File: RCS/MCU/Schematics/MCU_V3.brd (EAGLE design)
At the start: 100 x 78.7 mm, 26 parts, among them IC1 FT232RL, Q2 8 MHz, U1 ATMEGA328P_TQFP, X1 USB-A

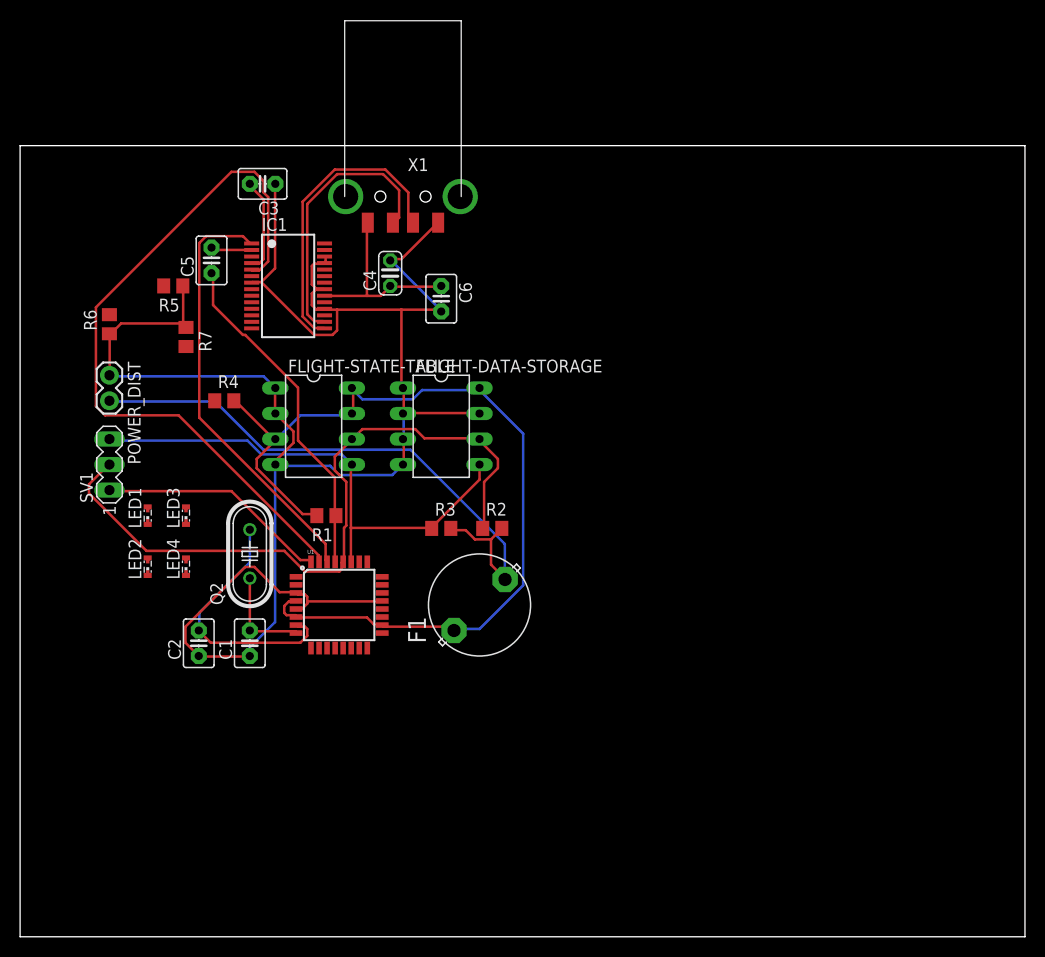
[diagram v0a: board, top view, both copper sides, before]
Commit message: Completed PCB layout
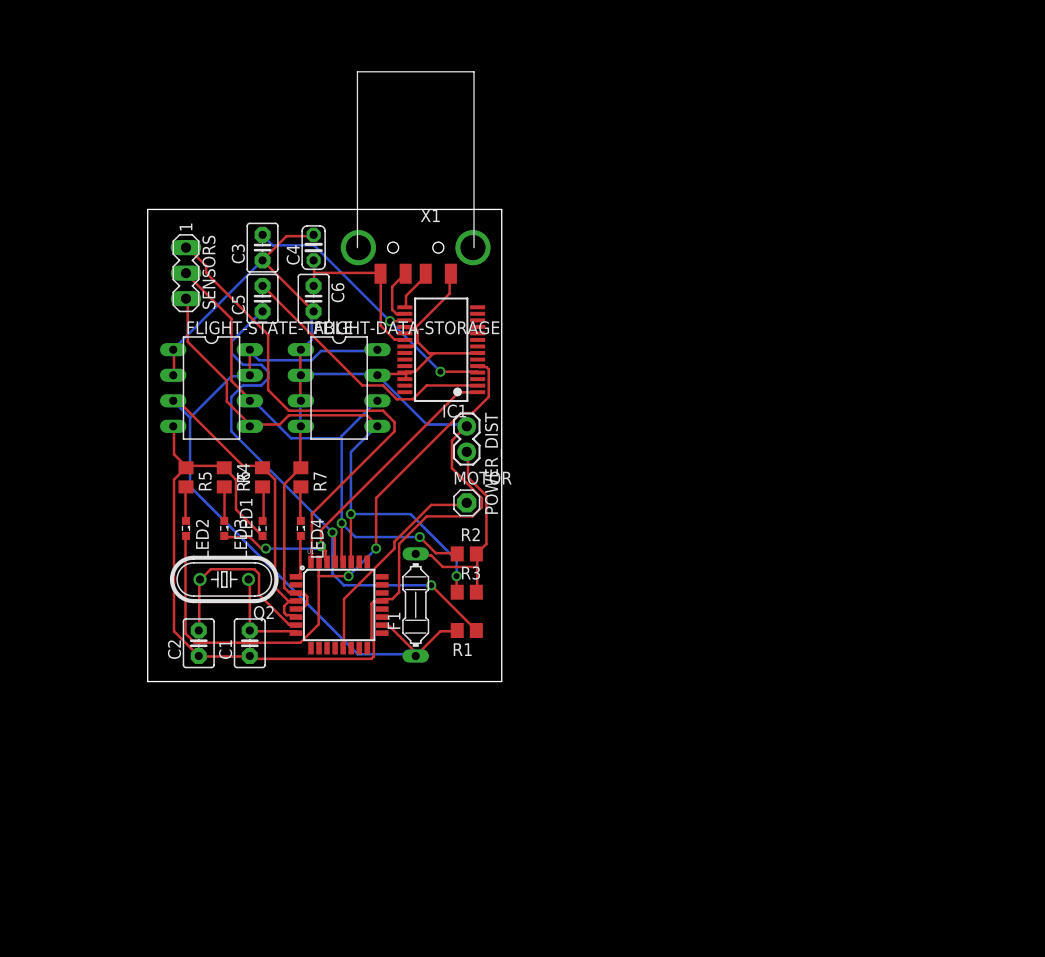
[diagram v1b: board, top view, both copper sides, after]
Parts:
- removed SV1: (no value), con-lstb:MA03-1
- added MOTOR: (no value), adafruit:1X01
- added SENSORS: (no value), con-lstb:MA03-1
- F1: value 500 mA -> 500mA; device fuse:19559 -> fuse:PICOFUSE
- LED1, LED2, LED3, LED4: device adafruit:SMARTLED-TTW -> eagle-ltspice:LED_SML0603
- moved POWER_DIST 35.9 mm to (44.5, 50.8)
- moved R5 19.1 mm to (16.5, 45.7), turned to 270 degrees
- moved R6 19.1 mm to (20.3, 45.7), turned to 270 degrees
- moved R7 18.1 mm to (27.9, 45.7)
- moved R1 18.1 mm to (44.5, 30.5)
- moved IC1 16.5 mm to (41.9, 58.4), turned to 90 degrees
- moved C6 12.7 mm to (29.2, 63.5)
- moved LED4 12.0 mm to (27.9, 40.6), turned to 270 degrees
- moved LED1 11.5 mm to (24.1, 40.6), turned to 90 degrees
- moved FLIGHT-STATE-TABLE 10.9 mm to (19.1, 54.6)
- moved FLIGHT-DATA-STORAGE 10.9 mm to (31.8, 54.6)
- moved R4 8.52 mm to (24.1, 45.7), turned to 90 degrees
- moved C4 8.03 mm to (29.2, 68.6)
- moved R3 6.84 mm to (44.5, 34.3)
- moved C3 6.35 mm to (24.1, 68.6), turned to 90 degrees
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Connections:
- new net MOTOR: MOTOR.1, U1.13
- net A4(SDA): now also SENSORS.3; no longer SV1.3
- net A5(SCL): now also SENSORS.2; no longer SV1.2
- net GND: now also LED1.C; no longer LED1.C@1
- net INT: now also SENSORS.1; no longer SV1.1
- net N$10: now also LED3.C; no longer LED3.C@1
- net N$4: now also LED4.A; no longer LED4.A@1
- net N$6: now also LED1.A; no longer LED1.A@1
- net N$8: now also LED4.C; no longer LED4.C@1
- net N$9: now also LED2.C; no longer LED2.C@1
- net RX: now also LED3.A; no longer LED3.A@1
- net TX: now also LED2.A; no longer LED2.A@1
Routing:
- net VDD: track 59.4 -> 22.0 mm
- net INT: track 23.1 -> 48.9 mm
- net DP: track 30.1 -> 4.34 mm
- net DTR: track 4.09 -> 26.6 mm
- net N$1: track 34.0 -> 56.4 mm, vias 0 -> 2
- net DM: track 27.6 -> 5.59 mm
- net MOTOR: track 0.00 -> 21.5 mm
- net N$7: track 9.47 -> 28.6 mm, vias 0 -> 2
- net A5(SCL): track 70.4 -> 56.4 mm, vias 0 -> 2
- net TX: track 71.7 -> 61.6 mm, vias 0 -> 2
- net N$5: track 92.3 -> 102.2 mm
- net A4(SDA): track 51.3 -> 59.2 mm, vias 0 -> 2
- net RX: track 42.8 -> 34.9 mm, vias 0 -> 2
- net N$2: track 25.7 -> 18.6 mm
- net N$4: track 0.00 -> 4.32 mm
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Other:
- board size 100 x 78.7 mm -> 35.2 x 47 mm

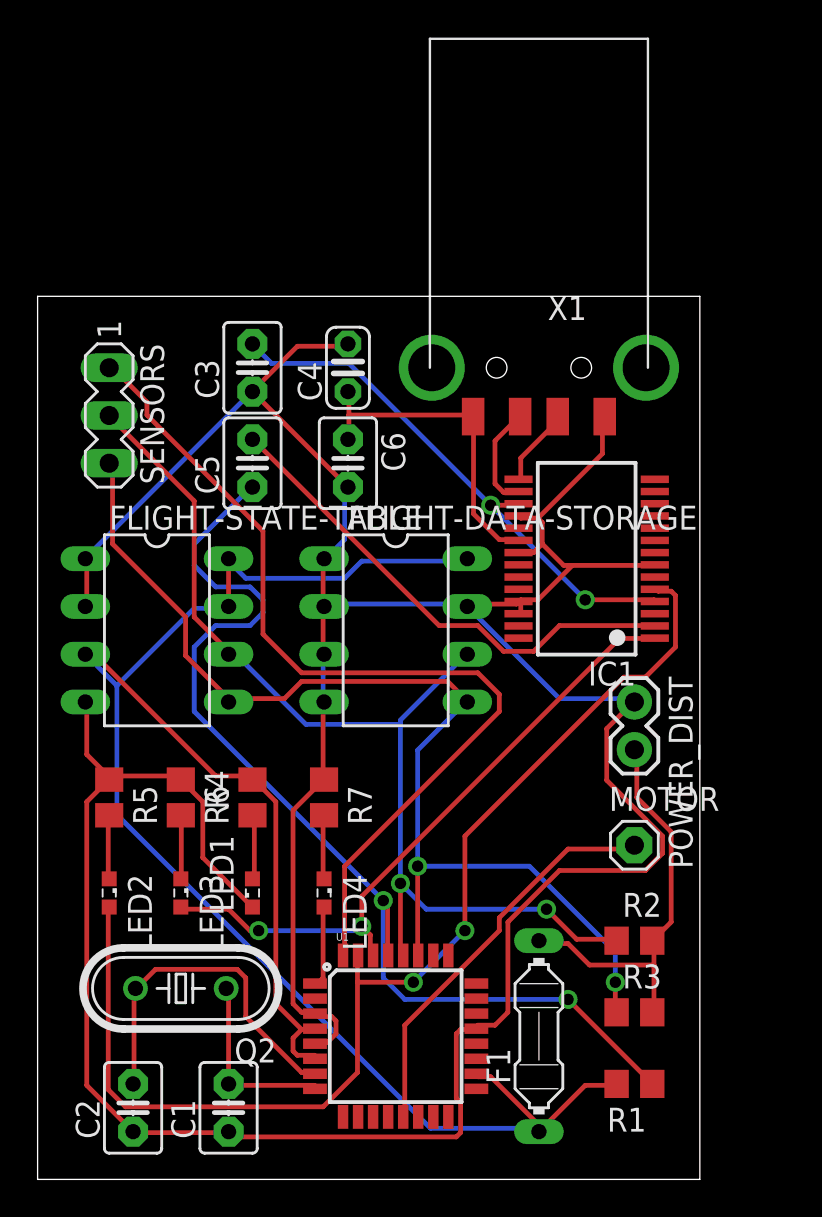
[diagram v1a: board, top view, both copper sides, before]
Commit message: Slightly updated schematic
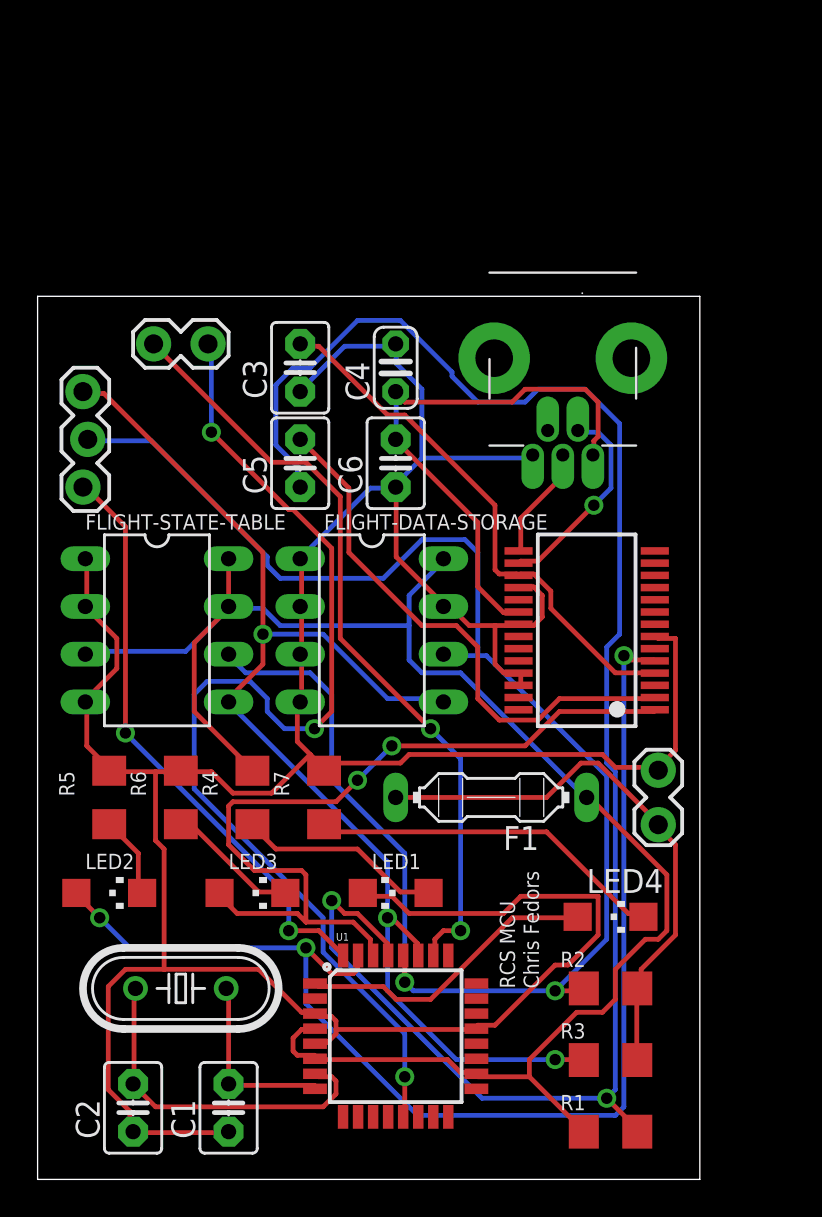
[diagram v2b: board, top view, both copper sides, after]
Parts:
- removed MOTOR: (no value), adafruit:1X01
- removed POWER_DIST: (no value), SparkFun-Connectors:1X02
- removed SENSORS: (no value), con-lstb:MA03-1
- removed X1: USB-A, adafruit:MOLEX_480371000
- added CN1: (no value), adafruit:USB-MINIB-THM-MOLEX
- added J1: MOTOR, SparkFun-Connectors:1X02_LOCK
- added J2: POWER, SparkFun-Connectors:1X02_LOCK
- added J3: SENSORS, SparkFun-Connectors:1X03_LOCK
- LED1, LED2, LED3, LED4: device eagle-ltspice:LED_SML0603 -> adafruit:CHIPLED_1206
- R1, R2, R3, R4, R5, R6, R7: device resistor:R0805 -> adafruit:R1206
- moved LED4 15.3 mm to (43.2, 39.4)
- moved F1 13.0 mm to (36.8, 45.7), turned to 180 degrees
- moved LED1 7.62 mm to (31.8, 40.6)
- moved IC1 3.81 mm to (41.9, 54.6)
- moved LED3 3.81 mm to (24.1, 40.6)
- moved R1 2.84 mm to (43.2, 27.9)
- moved R2 2.84 mm to (43.2, 35.6)
- moved R3 2.84 mm to (43.2, 31.8)
- moved C3 2.54 mm to (26.7, 68.6)
- moved C5 2.54 mm to (26.7, 63.5)
- moved C4 2.54 mm to (31.8, 68.6)
- moved C6 2.54 mm to (31.8, 63.5)
- moved FLIGHT-DATA-STORAGE 1.27 mm to (30.5, 54.6)
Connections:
- new net FEEDBACK: J1.1, U1.26
- net A4(SDA): now also J3.3; no longer SENSORS.3
- net A5(SCL): now also J3.2; no longer SENSORS.2
- net DM: now also CN1.D-; no longer X1.2
- net DP: now also CN1.D+; no longer X1.3
- net GND: now also CN1.GND, J2.1; no longer POWER_DIST.1, X1.4
- net INT: now also J3.1; no longer SENSORS.1
- net MOTOR: now also J1.2; no longer MOTOR.1
- net USBVDD: now also CN1.VBUS; no longer X1.1
- net VDD: now also J2.2; no longer POWER_DIST.2
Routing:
- net FEEDBACK: track 0.00 -> 41.5 mm, vias 0 -> 2
- net MOTOR: track 21.5 -> 59.0 mm, vias 0 -> 3
- net N$1: track 56.4 -> 92.7 mm
- net A5(SCL): track 56.4 -> 89.2 mm
- net INT: track 48.9 -> 31.7 mm, vias 0 -> 2
- net N$8: track 3.39 -> 19.1 mm
- net USBVDD: track 17.3 -> 29.5 mm
- net N$4: track 4.32 -> 16.1 mm
- net N$5: track 102.2 -> 91.0 mm
- net GND: track 193.4 -> 183.4 mm
- net RX: track 34.9 -> 44.2 mm
- net VDD: track 22.0 -> 29.9 mm
- net N$6: track 3.43 -> 10.9 mm
- net A4(SDA): track 59.2 -> 66.6 mm, vias 2 -> 3
- net DM: track 5.59 -> 10.9 mm, vias 0 -> 1
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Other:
- board text added: "Chris Fedors"
- board text added: "RCS MCU"
